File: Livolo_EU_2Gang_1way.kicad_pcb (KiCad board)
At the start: 2 copper layers, 43 x 43 mm, 39 parts, among them IC1 ATMEGA328P, U1 ATSHA204A, U2 RFM69_MINIMAL

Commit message: update gerber
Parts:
- moved U$5 0.19 mm to (134.6, 105.1)
- moved U$1 0.18 mm to (162.2, 105.0)
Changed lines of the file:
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@@
     (links 100)
     (no_connects 0)
-    (area 126.926099 83.428599 170.076101 126.578601)
+    (area 124.46 78.24 172.720001 139.426629)
     (thickness 1.6)
     (drawings 35)
@@
   )
   (module Livolo:touch_pad_16mm (layer Bottom)
-    (at 134.62 104.91)
+    (at 134.6 105.1)
     (fp_text reference U$5 (at -0.075 -0.85) (layer B.SilkS) hide
       (effects (font (size 0.4 0.4) (thickness 0.1)) (justify mirror))
@@
   )
   (module Livolo:touch_pad_16mm (layer Bottom)
-    (at 162.306 104.91)
+    (at 162.2 105.05)
     (fp_text reference U$1 (at -0.075 -0.85) (layer B.SilkS) hide
       (effects (font (size 0.4 0.4) (thickness 0.1)) (justify mirror))

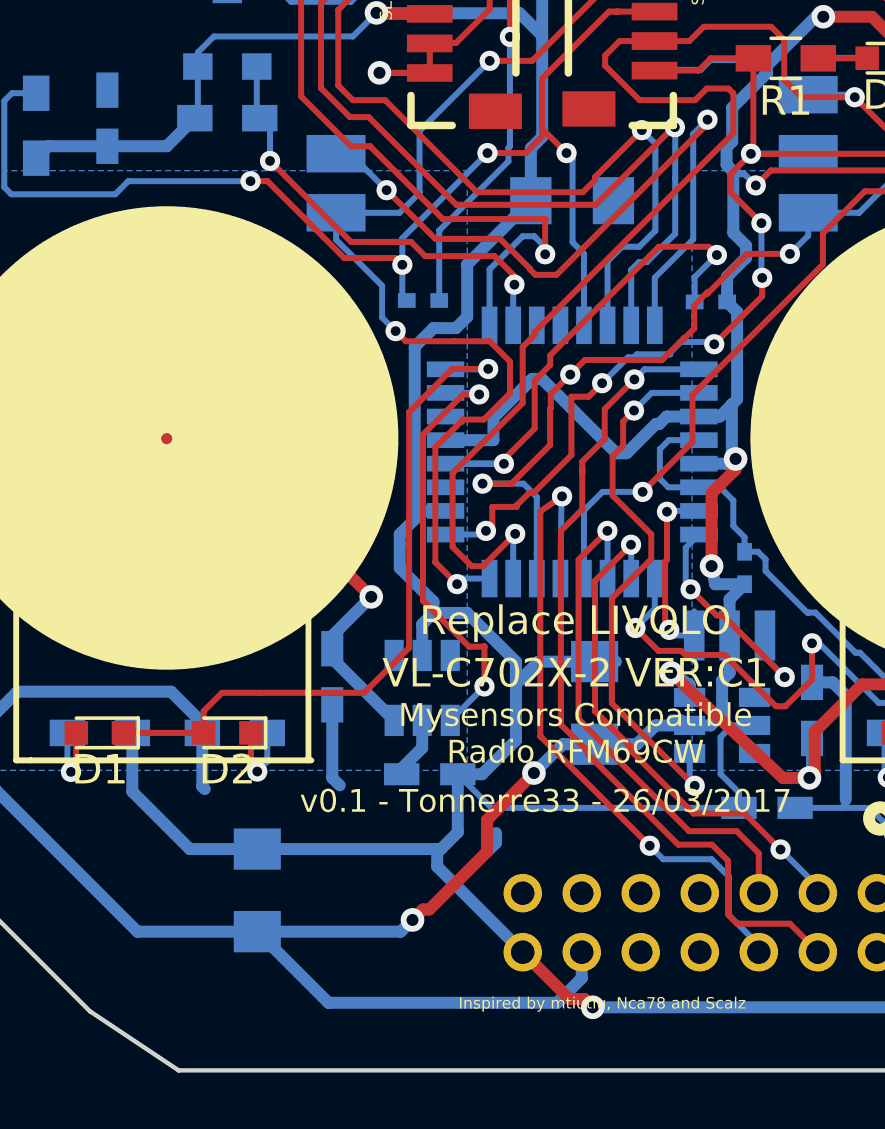
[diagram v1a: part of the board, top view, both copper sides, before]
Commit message: move capacitor C11
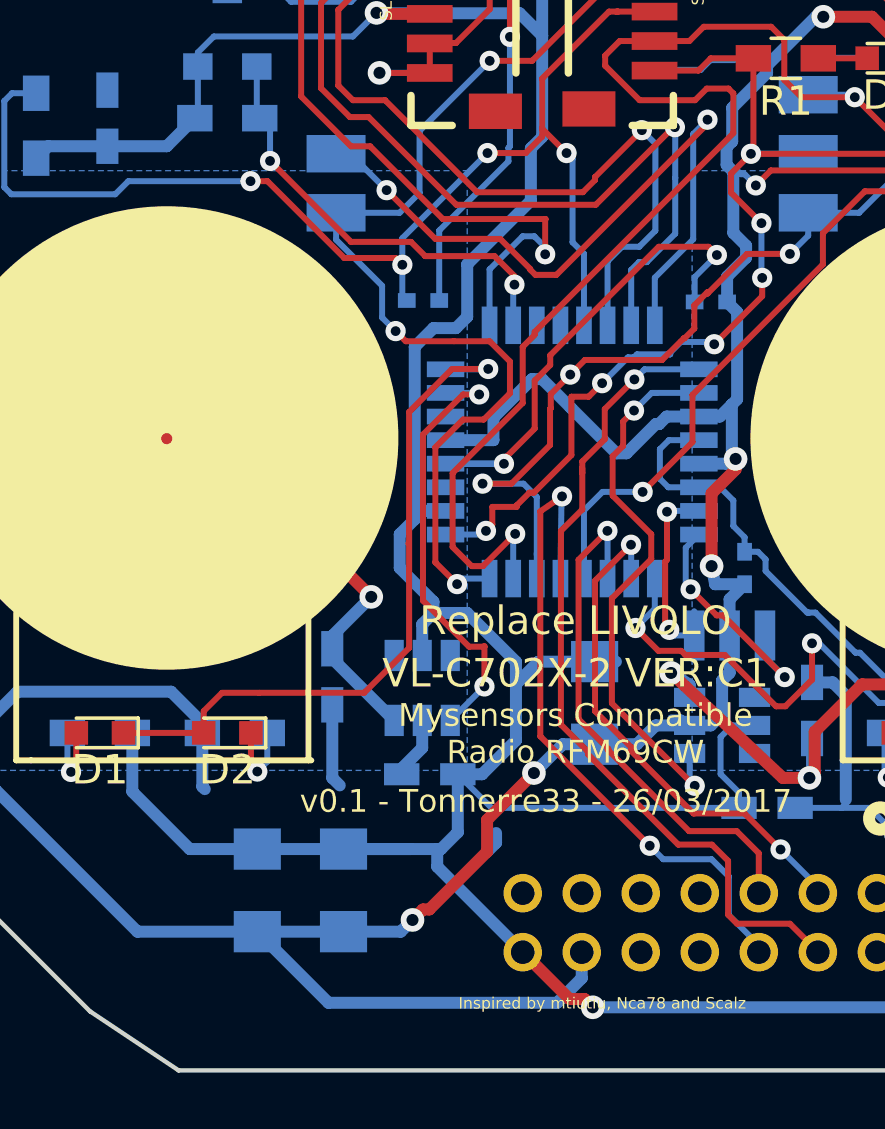
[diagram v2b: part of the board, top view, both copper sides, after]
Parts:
- moved C11 24.6 mm to (140.6, 120.4), turned to 90 degrees
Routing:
- net VCC: track 175.6 -> 177.9 mm
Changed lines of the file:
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@@
     (thickness 1.6)
     (drawings 35)
-    (tracks 822)
+    (tracks 824)
     (zones 0)
     (modules 39)
@@
   )
   (module Livolo_EU_2Gang_1way:EIA3216 (layer Bottom)
-    (at 148.336 97.036 180)
+    (at 140.589 120.404 90)
     (descr "GENERIC EIA 3216 (1206) POLARIZED TANTALUM CAPACITOR")
     (tags "GENERIC EIA 3216 (1206) POLARIZED TANTALUM CAPACITOR")
     (attr smd)
-    (fp_text reference C11 (at 1.524 1.4478 180) (layer B.SilkS)
+    (fp_text reference C11 (at 1.524 1.4478 90) (layer B.SilkS)
       (effects (font (size 0.6096 0.6096) (thickness 0.127)) (justify mirror))
     )
-    (fp_text value 100u (at 1.8288 -0.8382 180) (layer B.SilkS)
+    (fp_text value 100u (at 1.8288 -0.8382 90) (layer B.SilkS)
       (effects (font (size 0.6096 0.6096) (thickness 0.127)) (justify mirror))
     )
@@
     (fp_line (start 2.09804 1.19888) (end 0.99822 1.19888) (layer Dwgs.User) (width 0.2032))
     (fp_line (start 2.413 0.762) (end 2.413 -0.762) (layer B.SilkS) (width 0.2032))
-    (pad + smd rect (at 1.39954 0 90) (size 1.59766 1.39954) (layers Bottom B.Paste B.Mask)
-      (net 2 VCC))
-    (pad - smd rect (at -1.39954 0 90) (size 1.59766 1.39954) (layers Bottom B.Paste B.Mask)
+    (pad + smd rect (at 1.39954 0) (size 1.59766 1.39954) (layers Bottom B.Paste B.Mask)
+      (net 2 VCC))
+    (pad - smd rect (at -1.39954 0) (size 1.59766 1.39954) (layers Bottom B.Paste B.Mask)
       (net 1 GND))
   )
@@
   (segment (start 153.67 111.768) (end 153.67 110.54) (width 0.4064) (layer Bottom) (net 1))
   (segment (start 153.67 110.54) (end 154.178 110.032) (width 0.4064) (layer Bottom) (net 1))
+  (segment (start 140.589 119.00446) (end 142.87246 119.00446) (width 0.4064) (layer Bottom) (net 2) (status 400000))
   (segment (start 156.3624 110.9933) (end 156.2989 110.9933) (width 0.2032) (layer Bottom) (net 2))
   (segment (start 157.9372 112.3522) (end 156.5783 110.9933) (width 0.2032) (layer Bottom) (net 2))
@@
   (segment (start 143.764 119.00446) (end 143.764 119.60198) (width 0.4064) (layer Bottom) (net 2))
   (segment (start 143.764 119.60198) (end 146.661 122.49898) (width 0.4064) (layer Bottom) (net 2))
-  (segment (start 137.668 119.00446) (end 143.764 119.00446) (width 0.4064) (layer Bottom) (net 2))
+  (segment (start 137.668 119.00446) (end 142.87246 119.00446) (width 0.4064) (layer Bottom) (net 2))
+  (segment (start 142.87246 119.00446) (end 143.764 119.00446) (width 0.4064) (layer Bottom) (net 2))
   (segment (start 143.764 119.00446) (end 143.89354 119.00446) (width 0.4064) (layer Bottom) (net 2))
   (segment (start 144.461 118.437) (end 144.461 116.471) (width 0.4064) (layer Bottom) (net 2))

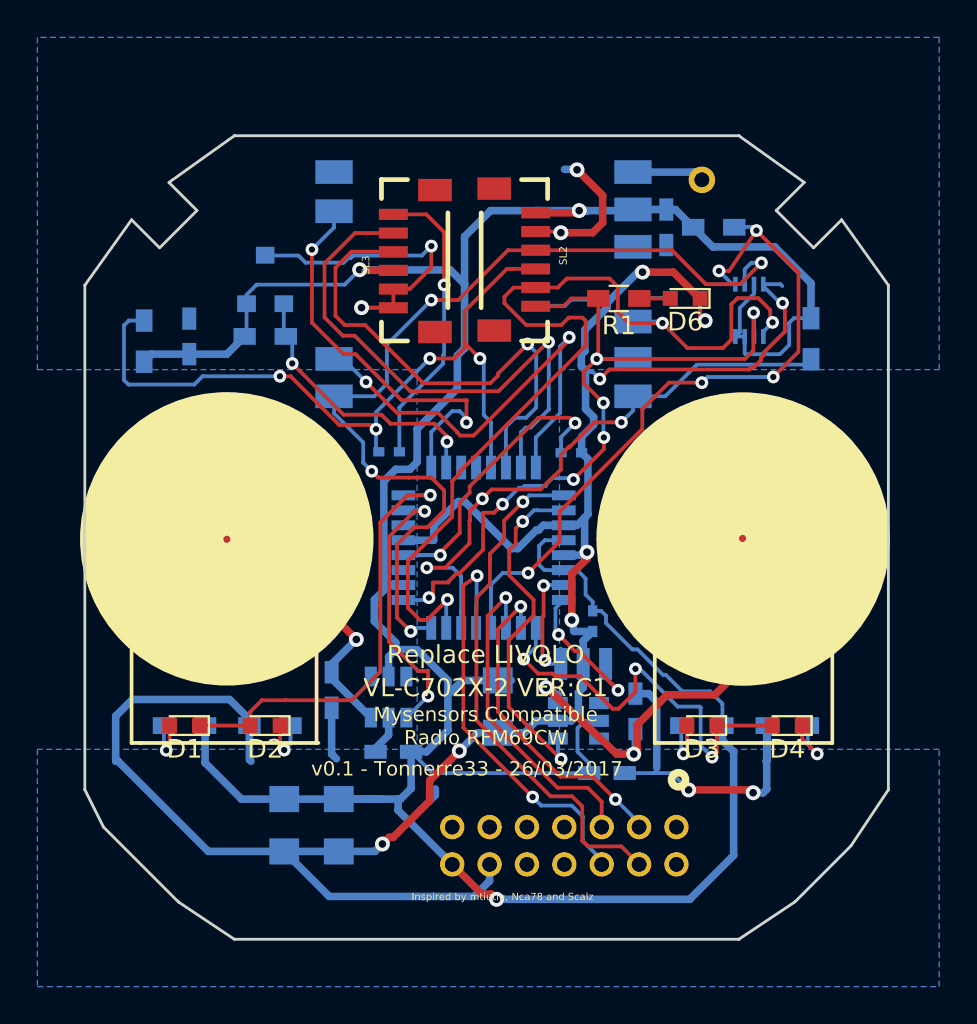
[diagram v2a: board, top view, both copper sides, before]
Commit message: increase distance between pad and wire
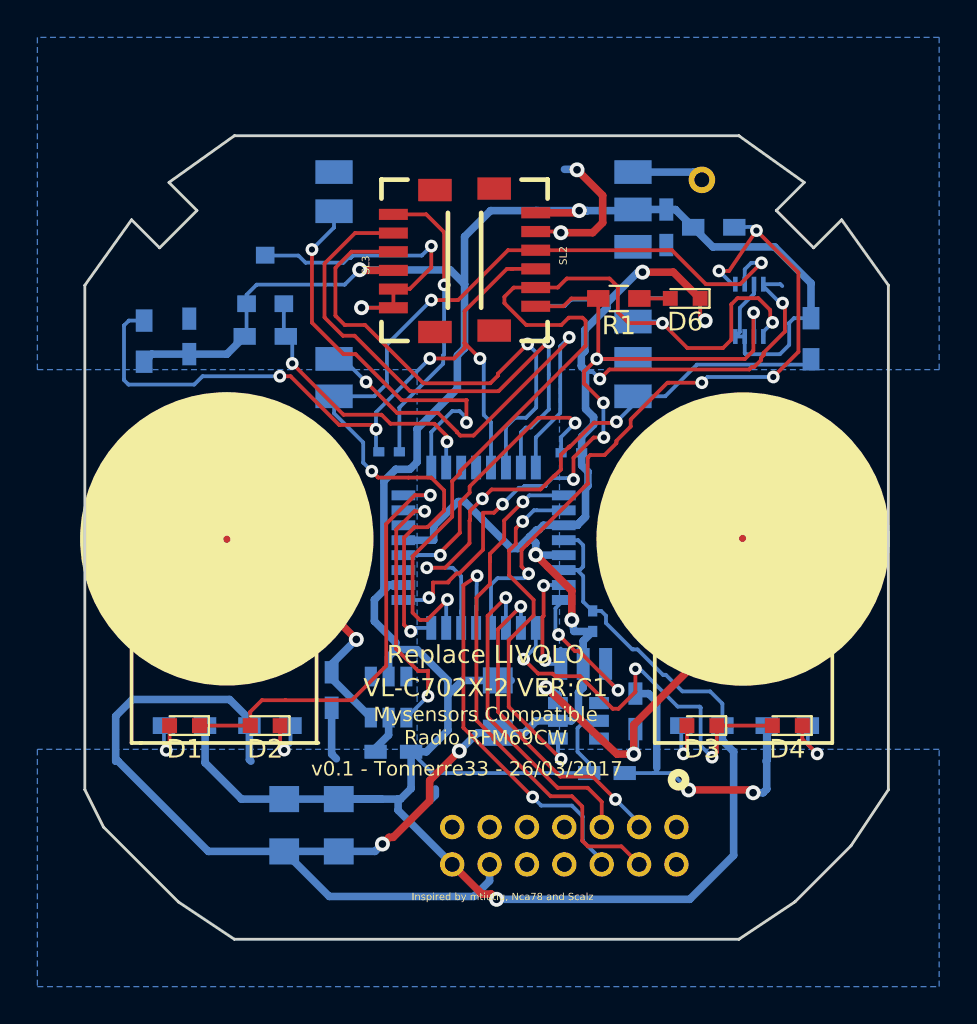
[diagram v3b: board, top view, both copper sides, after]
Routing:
- net /N$3: track 24.3 -> 22.6 mm
- net /FLASH_CS: track 38.5 -> 39.5 mm

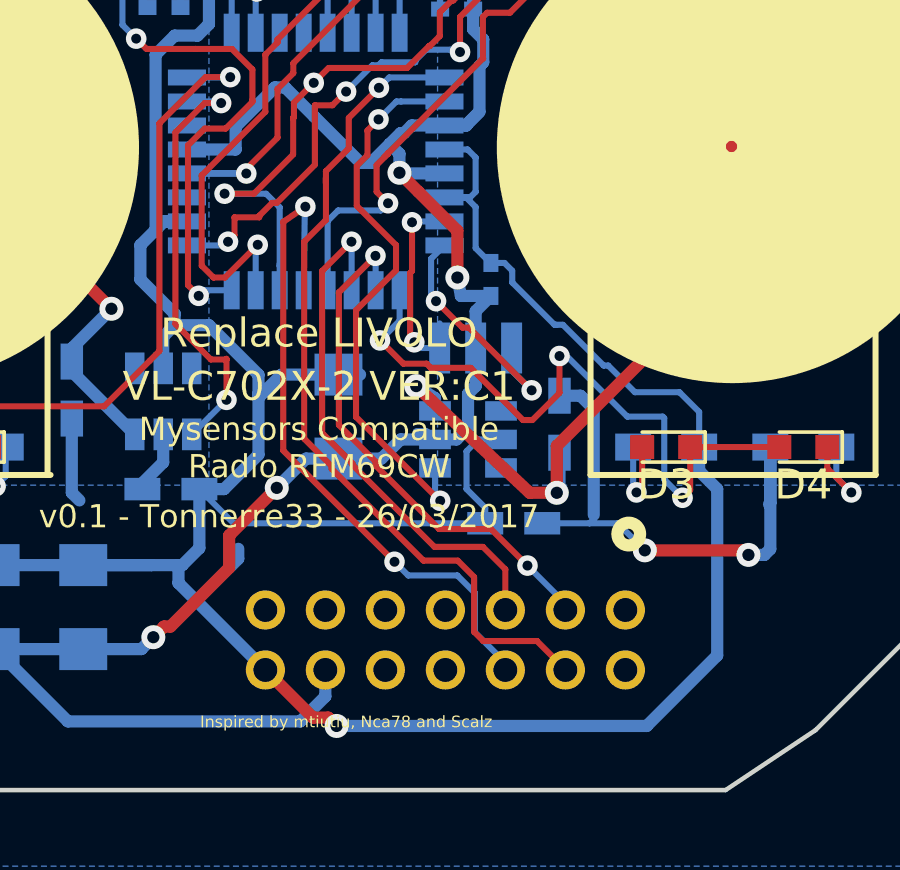
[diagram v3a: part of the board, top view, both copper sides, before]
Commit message: move 14 pins connector
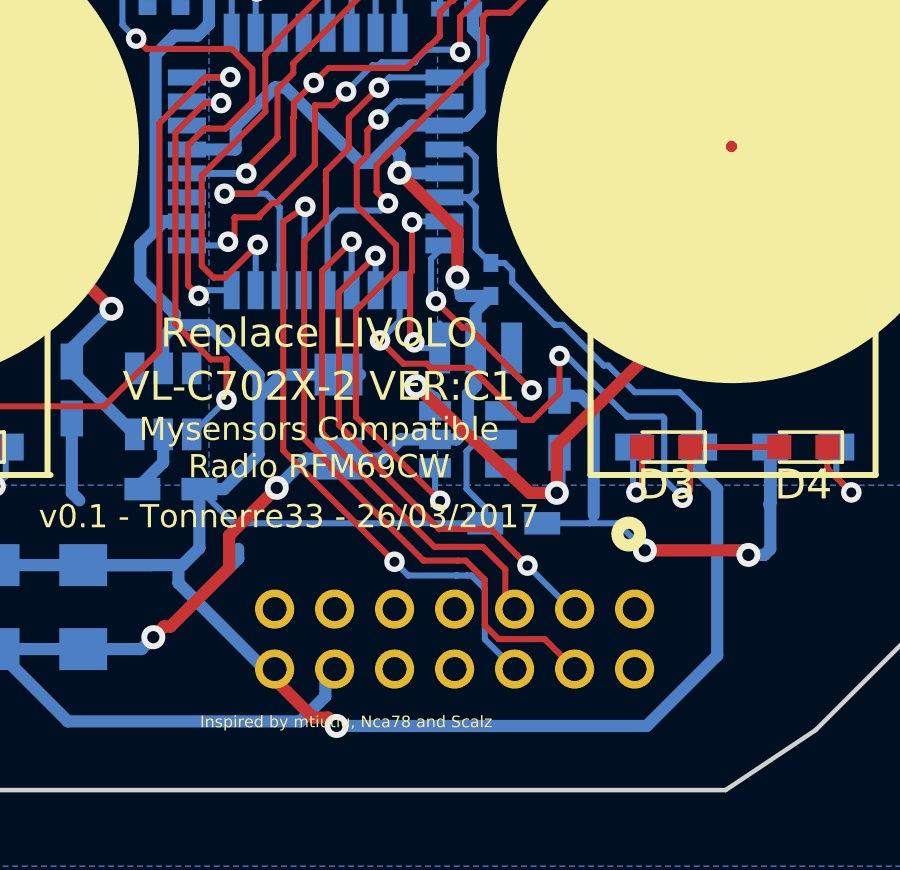
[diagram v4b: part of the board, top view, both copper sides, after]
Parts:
- moved U$2 0.31 mm to (145.7, 119.2)
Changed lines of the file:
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@@
     (thickness 1.6)
     (drawings 35)
-    (tracks 838)
+    (tracks 840)
     (zones 0)
     (modules 39)
@@
   )
   (module Livolo_EU_2Gang_1way:CONNECTOR_02_X_07_2MM (layer Bottom)
-    (at 145.391 119.23 270)
+    (at 145.7 119.2 270)
     (attr virtual)
     (fp_text reference U$2 (at 4.98348 1.36398 270) (layer B.SilkS)
@@
   (segment (start 151.13 105.926) (end 151.13 105.291) (width 0.4064) (layer Bottom) (net 1))
   (segment (start 151.13 105.291) (end 150.80615 104.96715) (width 0.4064) (layer Bottom) (net 1))
-  (segment (start 151.15178 105.94778) (end 152.6296 105.94778) (width 0.4064) (layer Bottom) (net 1) (status 800000))
+  (segment (start 151.15178 105.94778) (end 152.6296 105.94778) (width 0.4064) (layer Bottom) (net 1))
   (segment (start 151.13 105.926) (end 151.15178 105.94778) (width 0.4064) (layer Bottom) (net 1))
   (segment (start 153.924 102.243) (end 153.924 101.481) (width 0.4064) (layer Bottom) (net 1))
@@
   (segment (start 153.67 111.768) (end 153.67 110.54) (width 0.4064) (layer Bottom) (net 1))
   (segment (start 153.67 110.54) (end 154.178 110.032) (width 0.4064) (layer Bottom) (net 1))
-  (segment (start 152.6296 106.74788) (end 153.48312 106.74788) (width 0.2032) (layer Bottom) (net 2) (status 400000))
-  (segment (start 153.40222 105.15022) (end 152.6296 105.15022) (width 0.2032) (layer Bottom) (net 2) (status 800000))
+  (segment (start 152.6296 106.74788) (end 153.48312 106.74788) (width 0.2032) (layer Bottom) (net 2))
+  (segment (start 153.40222 105.15022) (end 152.6296 105.15022) (width 0.2032) (layer Bottom) (net 2))
   (segment (start 153.67 105.418) (end 153.40222 105.15022) (width 0.2032) (layer Bottom) (net 2))
   (segment (start 153.67 106.561) (end 153.67 105.418) (width 0.2032) (layer Bottom) (net 2))
@@
   (segment (start 156.2989 110.9933) (end 154.8892 109.5836) (width 0.2032) (layer Bottom) (net 2))
   (segment (start 154.3011 108.932) (end 154.178 108.932) (width 0.2032) (layer Bottom) (net 2))
-  (segment (start 154.178 108.932) (end 154.178 108.9486) (width 0.2032) (layer Bottom) (net 2) (status 400000))
+  (segment (start 154.178 108.932) (end 154.178 108.9486) (width 0.2032) (layer Bottom) (net 2))
   (segment (start 154.178 108.9486) (end 153.67 108.4406) (width 0.2032) (layer Bottom) (net 2))
   (segment (start 153.67 108.4406) (end 153.67 107.069) (width 0.2032) (layer Bottom) (net 2))
@@
   (segment (start 156.676 92.2136) (end 158.3274 92.2136) (width 0.2032) (layer Top) (net 14))
   (segment (start 158.3274 92.2136) (end 158.331 92.21) (width 0.2032) (layer Top) (net 14))
-  (segment (start 154.65946 122.25706) (end 153.6446 121.2422) (width 0.2032) (layer Bottom) (net 15))
+  (segment (start 153.3779 119.3499) (end 153.5303 119.3499) (width 0.2032) (layer Bottom) (net 15))
+  (segment (start 153.035 119.3499) (end 153.3779 119.3499) (width 0.2032) (layer Bottom) (net 15))
+  (segment (start 153.9748 121.47532) (end 154.96846 122.46898) (width 0.2032) (layer Bottom) (net 15))
+  (segment (start 153.9748 119.7944) (end 153.9748 121.47532) (width 0.2032) (layer Bottom) (net 15))
+  (segment (start 153.5303 119.3499) (end 153.9748 119.7944) (width 0.2032) (layer Bottom) (net 15))
   (segment (start 147.97632 107.07308) (end 147.93822 109.8416) (width 0.2032) (layer Bottom) (net 15))
   (segment (start 147.9931 107.0563) (end 147.97632 107.07308) (width 0.2032) (layer Bottom) (net 15))
@@
   (via (at 150.9649 118.8927) (size 0.6858) (drill 0.3302) (layers Top Bottom) (net 15))
   (segment (start 151.4221 119.3499) (end 150.9649 118.8927) (width 0.2032) (layer Bottom) (net 15))
-  (segment (start 153.0604 119.3499) (end 151.4221 119.3499) (width 0.2032) (layer Bottom) (net 15))
-  (segment (start 153.6446 119.9341) (end 153.0604 119.3499) (width 0.2032) (layer Bottom) (net 15))
-  (segment (start 153.6446 121.2422) (end 153.6446 119.9341) (width 0.2032) (layer Bottom) (net 15))
-  (segment (start 154.65946 122.49898) (end 154.65946 122.25706) (width 0.2032) (layer Bottom) (net 15))
+  (segment (start 153.0604 119.3499) (end 153.035 119.3499) (width 0.2032) (layer Bottom) (net 15))
+  (segment (start 153.035 119.3499) (end 151.4221 119.3499) (width 0.2032) (layer Bottom) (net 15))
+  (segment (start 153.0731 118.8546) (end 153.3398 118.8546) (width 0.2032) (layer Top) (net 16))
+  (segment (start 148.6789 106.2689) (end 148.6789 107.5008) (width 0.2032) (layer Top) (net 16))
+  (segment (start 147.955 108.2247) (end 148.6789 107.5008) (width 0.2032) (layer Top) (net 16))
+  (segment (start 147.955 114.7906) (end 147.955 108.2247) (width 0.2032) (layer Top) (net 16))
+  (segment (start 148.8694 115.705) (end 147.955 114.7906) (width 0.2032) (layer Top) (net 16))
+  (segment (start 148.8694 115.7939) (end 148.8694 115.705) (width 0.2032) (layer Top) (net 16))
+  (segment (start 151.9301 118.8546) (end 148.8694 115.7939) (width 0.2032) (layer Top) (net 16))
+  (segment (start 153.0731 118.8546) (end 151.9301 118.8546) (width 0.2032) (layer Top) (net 16))
+  (segment (start 155.9718 121.4708) (end 156.96998 122.46898) (width 0.2032) (layer Top) (net 16))
+  (segment (start 154.432 121.4708) (end 155.9718 121.4708) (width 0.2032) (layer Top) (net 16))
+  (segment (start 153.9748 121.0136) (end 154.432 121.4708) (width 0.2032) (layer Top) (net 16))
+  (segment (start 153.9748 119.4896) (end 153.9748 121.0136) (width 0.2032) (layer Top) (net 16))
+  (segment (start 153.3398 118.8546) (end 153.9748 119.4896) (width 0.2032) (layer Top) (net 16))
   (segment (start 149.4409 105.1132) (end 149.4409 104.0972) (width 0.2032) (layer Top) (net 16))
   (segment (start 148.6789 105.8752) (end 149.4409 105.1132) (width 0.2032) (layer Top) (net 16))
@@
   (via (at 150.4442 103.0939) (size 0.6858) (drill 0.3302) (layers Top Bottom) (net 16))
   (segment (start 149.4409 104.0972) (end 150.4442 103.0939) (width 0.2032) (layer Top) (net 16))
-  (segment (start 156.66098 122.49898) (end 156.66098 122.48058) (width 0.2032) (layer Top) (net 16))
-  (segment (start 156.66098 122.48058) (end 155.7147 121.5343) (width 0.2032) (layer Top) (net 16))
-  (segment (start 155.7147 121.5343) (end 153.924 121.5343) (width 0.2032) (layer Top) (net 16))
-  (segment (start 153.924 121.5343) (end 153.6192 121.2295) (width 0.2032) (layer Top) (net 16))
-  (segment (start 153.6192 121.2295) (end 153.6192 119.4007) (width 0.2032) (layer Top) (net 16))
-  (segment (start 153.6192 119.4007) (end 153.0731 118.8546) (width 0.2032) (layer Top) (net 16))
-  (segment (start 153.0731 118.8546) (end 151.9301 118.8546) (width 0.2032) (layer Top) (net 16))
-  (segment (start 151.9301 118.8546) (end 148.8694 115.7939) (width 0.2032) (layer Top) (net 16))
-  (segment (start 148.8694 115.7939) (end 148.8694 115.705) (width 0.2032) (layer Top) (net 16))
-  (segment (start 148.8694 115.705) (end 147.955 114.7906) (width 0.2032) (layer Top) (net 16))
-  (segment (start 147.955 114.7906) (end 147.955 108.2247) (width 0.2032) (layer Top) (net 16))
-  (segment (start 147.955 108.2247) (end 148.6789 107.5008) (width 0.2032) (layer Top) (net 16))
-  (segment (start 148.6789 107.5008) (end 148.6789 106.2689) (width 0.2032) (layer Top) (net 16))
   (segment (start 148.6789 106.2689) (end 148.6789 106.0911) (width 0.2032) (layer Top) (net 16))
   (segment (start 152.47112 111.768) (end 151.8158 111.768) (width 0.2032) (layer Bottom) (net 17))
